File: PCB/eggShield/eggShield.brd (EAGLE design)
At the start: 68.6 x 53.3 mm, 19 parts

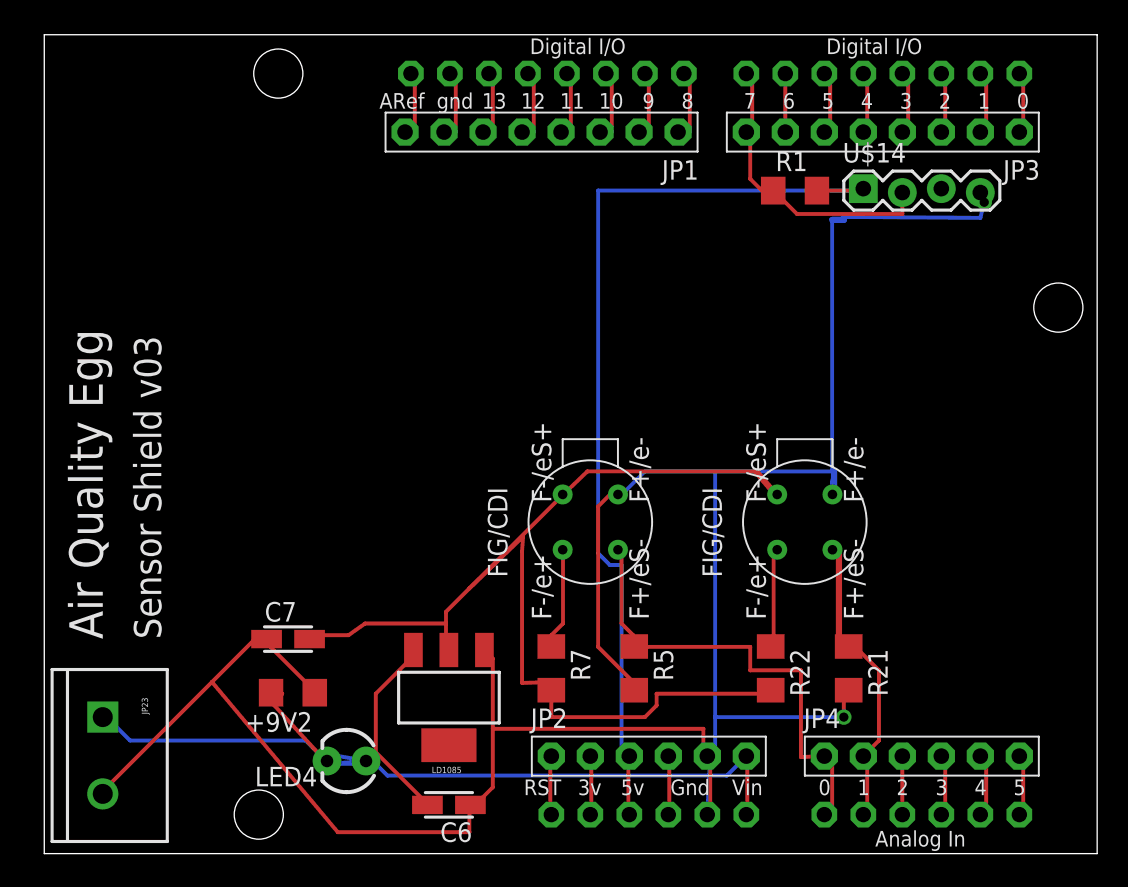
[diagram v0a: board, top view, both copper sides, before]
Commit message: updates to the layout and schematics, bringing in elements of the CMOS breakout module
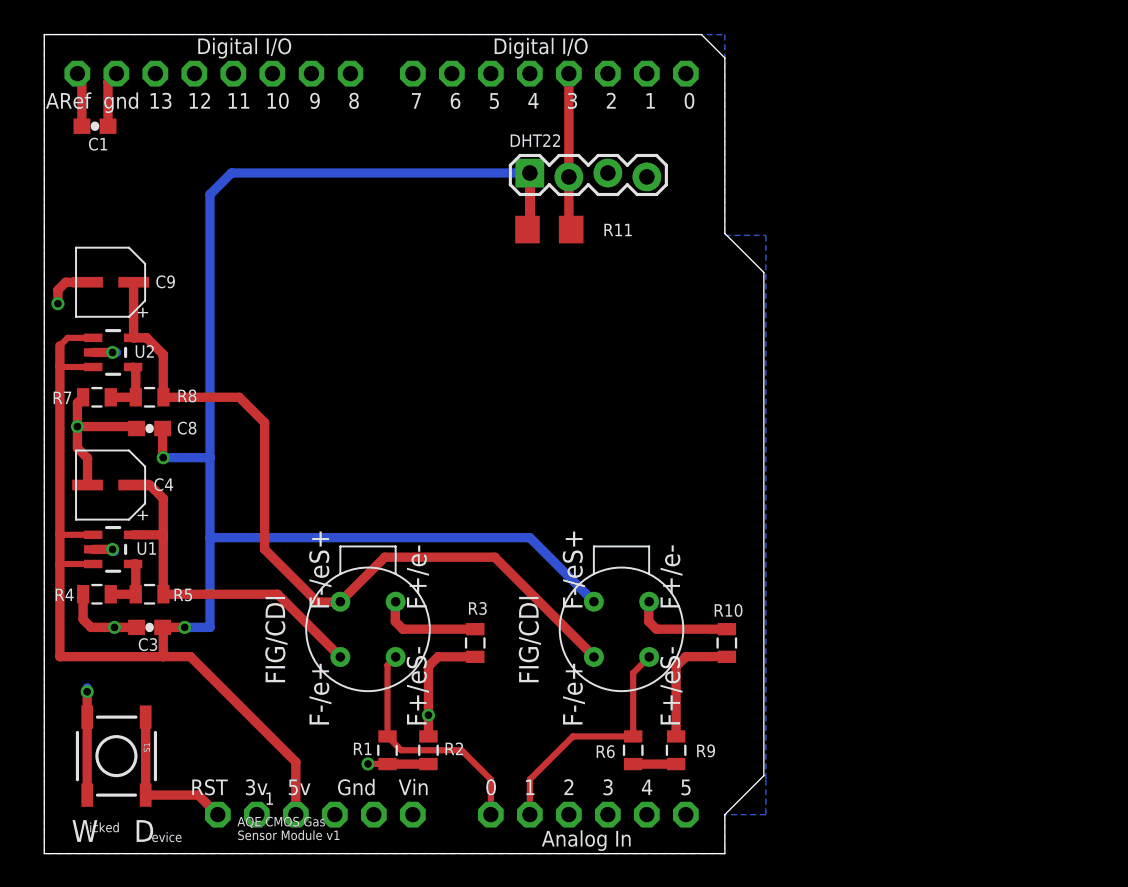
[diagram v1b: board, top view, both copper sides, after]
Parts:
- removed +9V2: 900 ohm, rcl:R1206
- removed C6, C7: 10uF, resistor:CT3216
- removed JP1, JP3: (no value), adafruit:1X08-BIG
- removed JP2, JP4: (no value), adafruit:1X06-BIG
- removed JP23: Screw Terminal, SparkFun:SCREWTERMINAL-5MM-2
- removed LD1085: V_REG_317SMD, SparkFun:SOT223
- removed LED4: (no value), SparkFun:LED3MM
- removed NO2: E2V NO2, ricardo:SR-4
- removed R21: 220k, rcl:R1206
- removed R22: 82 ohm, rcl:R1206
- removed U$13: E2V, ricardo:SR-4
- removed U$14: RHT03, ricardo:1X04_LOCK
- added C1, C3, C8: 0.1uF, SparkFun:0603-CAP
- added C4, C9: 10uF, wicked-device:TYPE-B_ALUMINUM_CAN
- added DHT22: RHT03, ricardo:1X04_LOCK
- added R10, R2, R3, R6, R9: (no value), SparkFun:0805
- added R11: 10k, rcl:R1206
- added R4: 150Ohm, SparkFun:0805
- added R8: 330Ohm, SparkFun:0805
- added S1: (no value), SparkFun:TACTILE_SWITCH_SMD
- added U$4: E2V, ricardo:SR-4
- added U$7: ARDUINO-NOHOLE, adafruit:ARDUINO-NOHOLE
- added U1, U2: V_REG_LDOSMD, SparkFun:SOT23-5
- R1: value 10k -> (none); device rcl:R1206 -> SparkFun:0805
- R5: value 220k -> 330Ohm; device rcl:R1206 -> SparkFun:0805
- R7: value 34 ohm -> 150Ohm; device rcl:R1206 -> SparkFun:0805
- U$2: value ARDUINO-NODIM -> E2V; device adafruit:ARDUINO-NODIM -> ricardo:SR-4
- moved R1 45.1 mm to (22.4, 6.73), turned to 90 degrees
- moved U$2 40.3 mm to (37.6, 14.6), turned to 90 degrees
- moved R7 34.5 mm to (3.43, 29.7), turned to 0 degrees
- moved R5 31.9 mm to (6.86, 16.9), turned to 0 degrees
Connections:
- removed net +5V: JP2.3, R1.2, U$14.VDD, U$2.5V
- removed net +9V: C6.+, JP2.6, JP23.1, LD1085.3, LED4.A, U$2.VIN
- removed net 1.8: +9V2.1, C6.-, C7.-, JP2.5, JP23.2, LD1085.1, NO2.FIGV+/E2V-, R21.2, R5.2, U$13.FIGV+/E2V-, U$14.GND, U$2.GND1
- removed net A3: JP3.8, R1.1, U$14.DATA, U$2.D7
- removed net N$10: JP4.4, U$2.A3
- removed net N$11: JP4.5, U$2.A4
- removed net N$12: JP4.6, U$2.A5
- removed net N$13: JP3.1, U$2.D0
- removed net N$14: JP3.2, U$2.D1
- removed net N$15: JP3.3, U$2.D2
- removed net N$16: JP3.4, U$2.D3
- removed net N$17: JP3.5, U$2.D4
- removed net N$18: JP3.6, U$2.D5
- removed net N$22: JP1.1, U$2.D8
- removed net N$23: JP1.2, U$2.D9
- removed net N$24: +9V2.2, LED4.K
- removed net N$25: JP1.3, U$2.D10
- removed net N$26: JP1.4, U$2.D11
- removed net N$27: JP1.5, U$2.D12
- removed net N$28: JP1.6, U$2.D13
- removed net N$29: JP1.7, U$2.GND
- removed net N$30: JP1.8, U$2.AREF
- removed net N$38: R22.1, U$13.FIGSIG/E2VH+
- removed net N$43: NO2.FIGSIG/E2VH+, R7.1
- removed net N$47: JP4.2, R21.1, U$13.FIGV+/E2VSIG, U$2.A1
- removed net N$5: JP3.7, U$2.D6
- removed net N$50: JP4.1, NO2.FIGV+/E2VSIG, R5.1, U$2.A0
- removed net N$55: JP4.3, U$2.A2
- removed net V+: C7.+, LD1085.2, NO2.FIGG/E2VS+, R22.2, R7.2, U$13.FIGG/E2VS+
- new net /CO_R1_SEL: R6.1, R9.2
- new net /CO_R2_SEL: R10.2, R9.1
- new net /NO2_R1_SEL: R1.1, R2.2
- new net /NO2_R2_SEL: R2.1, R3.2
- new net /RESET: S1.1, S1.2, U$7.RESET
- new net 1.7V: C4.P$1, R5.2, U$4.FIGSIG/E2VH+, U1.5
- new net 2.5V: C9.P$1, R8.2, U$2.FIGSIG/E2VH+, U$4.FIGG/E2VS+, U2.5
- new net 3V: U$7.3V
- new net CO_SENSE: R6.2, U$2.FIGV+/E2VSIG, U$7.A1
- new net D3: DHT22.DATA, R11.1, U$7.D3
- new net GND: C1.1, C3.1, C4.P$2, C8.1, C9.P$2, DHT22.GND, R10.1, R3.1, R4.1, R7.1, S1.3, S1.4, U$2.FIGV+/E2V-, U$4.FIGV+/E2V-, U$7.GND, U$7.GND1, U$7.GND2, U1.2, U2.2
- new net NO2_SENSE: R1.2, U$4.FIGV+/E2VSIG, U$7.A0
- new net SCL: U$7.A5
- new net SDA: U$7.A4
- new net VCC: C3.2, C8.2, DHT22.VDD, R11.2, U$2.FIGG/E2VS+, U$7.5V, U1.1, U1.3, U2.1, U2.3
- new net VIN: U$7.VIN
- net N$1: now also R4.2, R5.1, U1.4; no longer JP2.1, U$2.RESET
- net N$2: now also R7.2, R8.1, U2.4; no longer JP2.2, U$2.3V
- net N$4: now also C1.2, U$7.AREF; no longer JP2.4, U$2.GND2
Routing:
- net 1.8: track 169.6 -> 0.00 mm, vias 2 -> 0
- net VCC: track 0.00 -> 144.7 mm, vias 0 -> 2
- net V+: track 74.5 -> 0.00 mm
- net +9V: track 65.8 -> 0.00 mm
- net +5V: track 62.4 -> 0.00 mm
- net 2.5V: track 0.00 -> 51.2 mm
- net GND: track 0.00 -> 46.0 mm, vias 0 -> 6
- net N$50: track 30.6 -> 0.00 mm
- net 1.7V: track 0.00 -> 23.7 mm
- net N$47: track 20.3 -> 0.00 mm
- net A3: track 19.6 -> 0.00 mm
- net CO_SENSE: track 0.00 -> 15.8 mm
- net NO2_SENSE: track 0.00 -> 15.6 mm
- net /RESET: track 0.00 -> 10.3 mm
- net D3: track 0.00 -> 10.2 mm
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- added copper zone on layer 16, net GND
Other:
- board size 68.6 x 53.3 mm -> 46.9 x 53.3 mm
- board text added: "1"
- board text added: "AQE CMOS Gas"
- board text added: "C4"
- board text added: "C9"
- board text added: "D"
- board text added: "Sensor Module v1"
- board text added: "W"
- board text added: "evice"
- board text added: "icked"
- board text removed: "Air Quality Egg"
- board text removed: "Sensor Shield v03"

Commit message: added 2:1 I2C Multiplexer
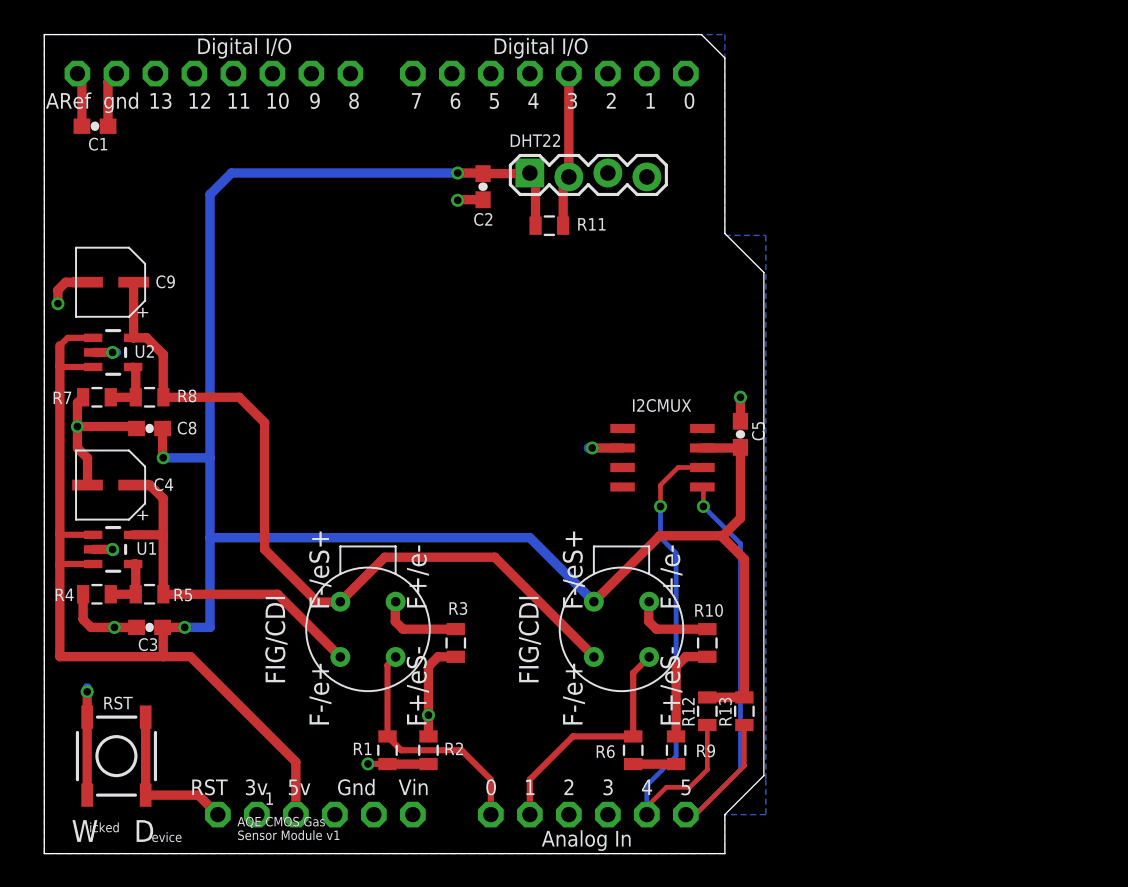
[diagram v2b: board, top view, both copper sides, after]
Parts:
- added C2, C5: 0.1uF, SparkFun:0603-CAP
- added I2CMUX: PCA9540BD, wicked-device:SO8
- added R12, R13: 4.7kOhm, SparkFun:0805
- R11: value 10k -> 10kOhm; device rcl:R1206 -> SparkFun:0805
- moved R10 1.27 mm to (43.2, 13.7)
- moved R3 1.27 mm to (26.8, 13.7)
- moved R11 0.25 mm to (32.9, 40.9), turned to 0 degrees
- renumbered S1 to RST
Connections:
- net D3: now also R11.2; no longer R11.1
- net GND: now also C2.1, C5.1, I2CMUX.6
- net SCL: now also I2CMUX.1, R13.1
- net SDA: now also I2CMUX.2, R12.1
- net VCC: now also C2.2, C5.2, I2CMUX.3, R11.1, R12.2, R13.2; no longer R11.2
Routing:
- net SDA: track 0.00 -> 34.2 mm, vias 0 -> 1
- net SCL: track 0.00 -> 32.0 mm, vias 0 -> 1
- net VCC: track 144.7 -> 175.6 mm, vias 2 -> 3
- net GND: track 46.0 -> 49.2 mm, vias 6 -> 9
- net /CO_R2_SEL: track 8.13 -> 6.86 mm
- net /NO2_R2_SEL: track 7.87 -> 6.60 mm

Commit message: rearranged some layout and routing to improve power filtering
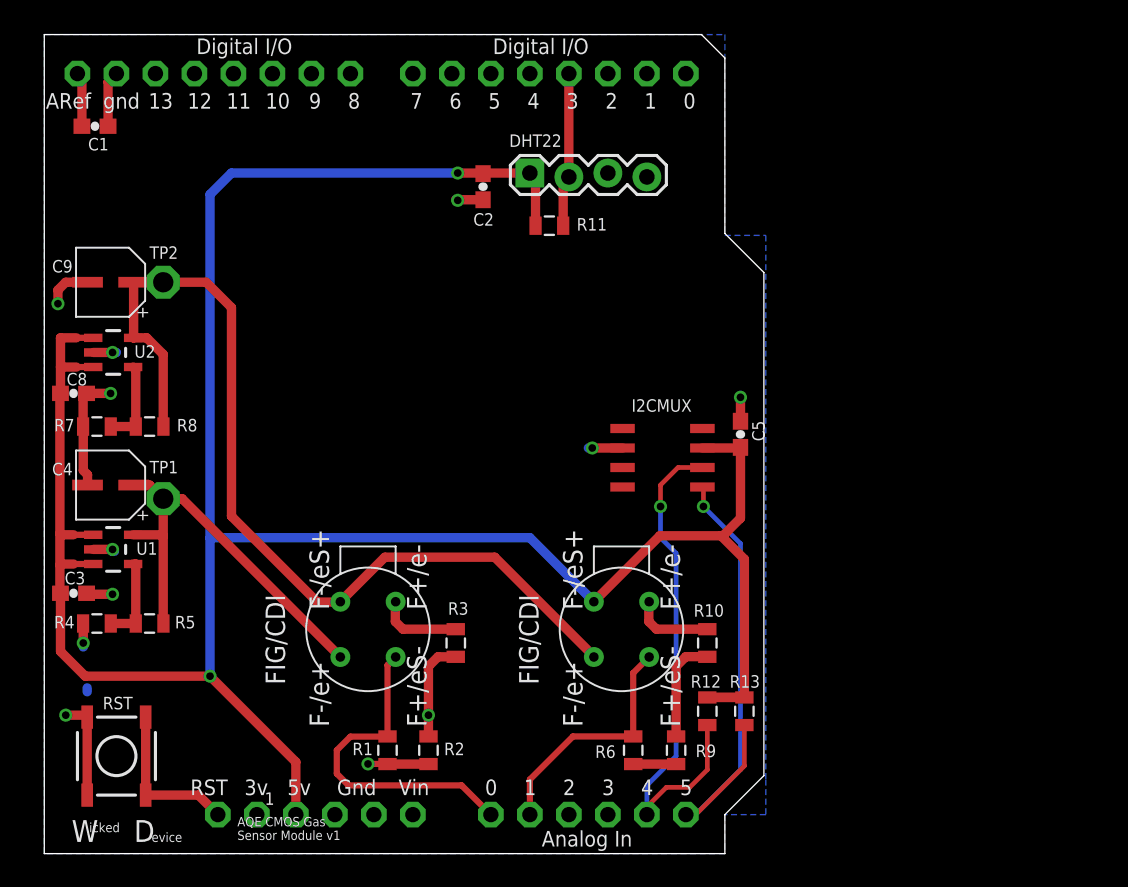
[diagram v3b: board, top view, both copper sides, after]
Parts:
- added TP1, TP2: TPPAD1-13, testpad:P1-13
- R12, R13: value 4.7kOhm -> 1.8kOhm
- moved C8 5.46 mm to (1.91, 30.0), turned to 180 degrees
- moved C3 5.43 mm to (1.91, 17.0), turned to 180 degrees
- moved R7 1.91 mm to (3.43, 27.8)
- moved R8 1.91 mm to (6.86, 27.8)
- moved R4 1.90 mm to (3.43, 15.0)
- moved R5 1.90 mm to (6.86, 15.0)
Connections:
- net 1.7V: now also TP1.TP
- net 2.5V: now also TP2.TP
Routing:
- net 2.5V: track 51.2 -> 61.3 mm
- net VCC: track 175.6 -> 168.9 mm, vias 3 -> 2
- net NO2_SENSE: track 15.6 -> 21.7 mm
- net GND: track 49.2 -> 44.6 mm, vias 9 -> 10
- net 1.7V: track 23.7 -> 28.2 mm
- net N$2: track 3.67 -> 5.58 mm
- net N$1: track 3.82 -> 5.73 mm

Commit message: some minor changes to component placement, routing, and silk screen
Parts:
- moved TP1 1.02 mm to (8.76, 23.1)
- moved TP2 1.02 mm to (8.76, 37.2)
- moved C2 0.64 mm to (29.2, 43.4)
- moved DHT22 0.64 mm to (32.3, 44.2)
- moved R2 0.64 mm to (25.7, 6.73)
- moved C4 0.64 mm to (4.95, 24.0)
- moved C9 0.64 mm to (4.95, 37.2)
- moved R5 0.64 mm to (7.49, 15.0)
- moved R8 0.64 mm to (7.49, 27.8)
- moved R4 0.64 mm to (4.06, 15.0)
- moved R7 0.64 mm to (4.06, 27.8)
- moved C3 0.64 mm to (2.54, 17.0)
- moved C8 0.64 mm to (2.54, 30.0)
- moved C1 0.63 mm to (3.94, 47.4)
- moved RST 0.63 mm to (5.33, 6.35)
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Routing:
- net SDA: track 34.2 -> 34.8 mm
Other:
- board size 46.9 x 53.3 mm -> 47.5 x 53.3 mm
- board text added: "1.7V"
- board text added: "2.5V"
- board text added: "Air Quality Egg"
- board text added: "Sensor Interface Shield v1"
- board text removed: "AQE CMOS Gas"
- board text removed: "Sensor Module v1"

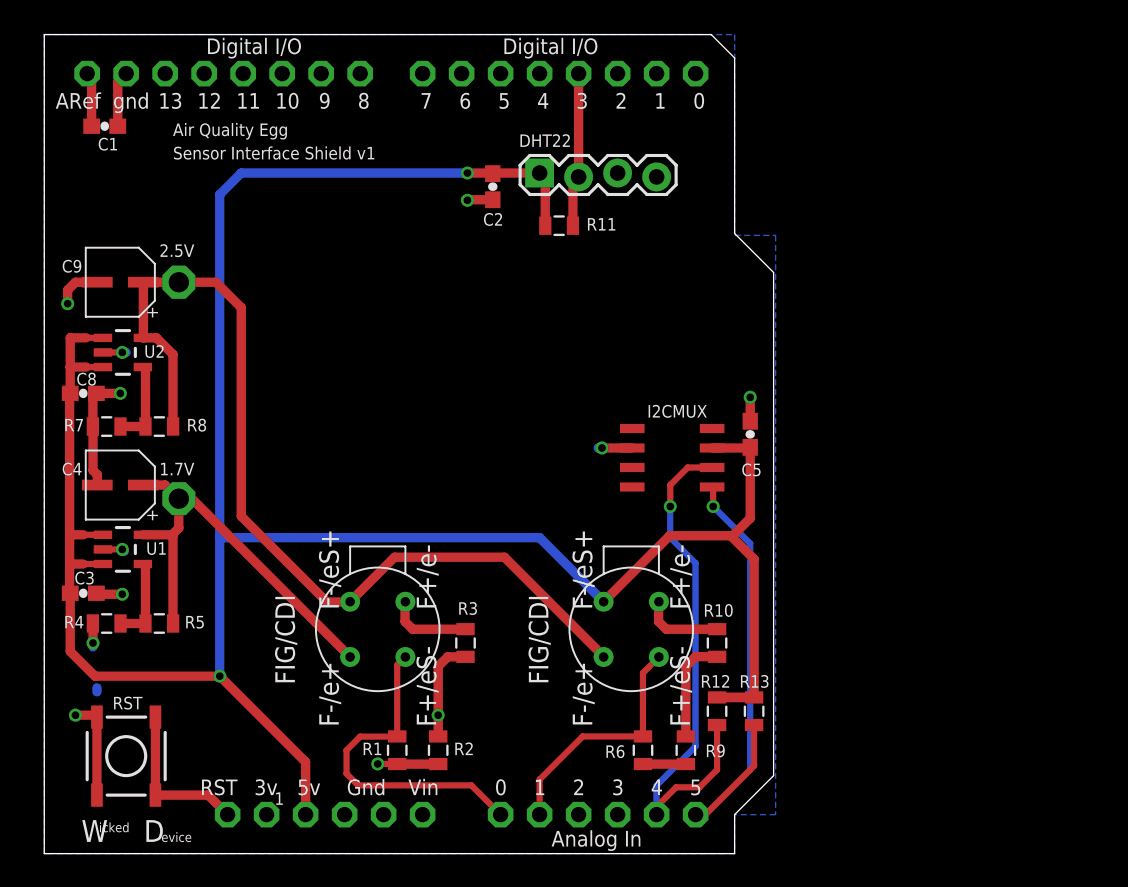
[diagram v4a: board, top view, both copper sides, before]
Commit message: added 4-pin connectors, needs to be checked against cabling; also noticed the range selection resistor taps need to be routed to arduino pins as well
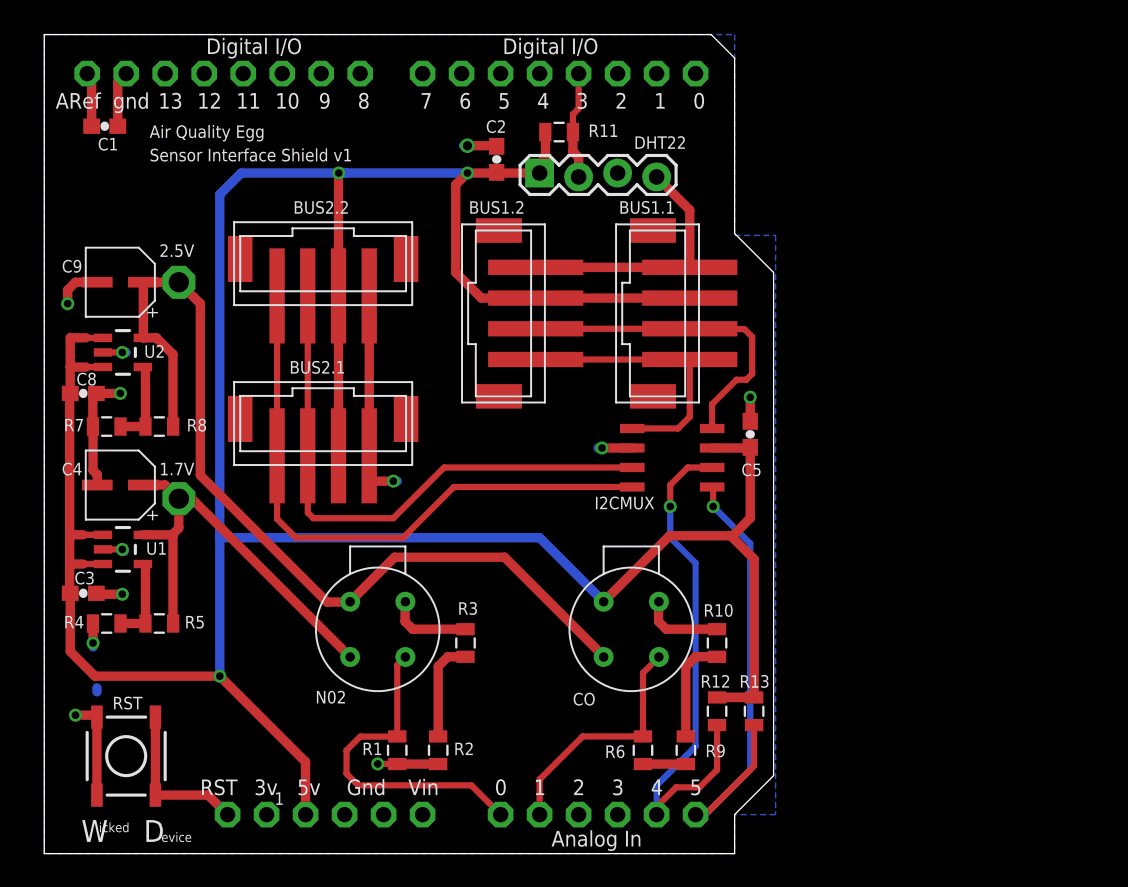
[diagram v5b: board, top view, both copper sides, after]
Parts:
- added BUS1.1, BUS1.2, BUS2.1, BUS2.2: 4-PIN-SMT, wicked-device:1775470-4
- moved R11 6.10 mm to (33.5, 47.0)
- moved C2 1.80 mm to (29.5, 45.2), turned to 270 degrees
- renumbered U$2 to CO, U$4 to N02
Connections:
- new net SCL0: BUS1.1.1, BUS1.2.1, I2CMUX.5
- new net SCL1: BUS2.1.1, BUS2.2.1, I2CMUX.8
- new net SDA0: BUS1.1.2, BUS1.2.2, I2CMUX.4
- new net SDA1: BUS2.1.2, BUS2.2.2, I2CMUX.7
- net GND: now also BUS1.1.4, BUS1.2.4, BUS2.1.4, BUS2.2.4
- net VCC: now also BUS1.1.3, BUS1.2.3, BUS2.1.3, BUS2.2.3
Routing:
- net VCC: track 168.9 -> 209.2 mm, vias 2 -> 3
- net SCL1: track 0.00 -> 39.5 mm
- net SDA1: track 0.00 -> 36.8 mm
- net GND: track 44.6 -> 75.6 mm, vias 10 -> 11
- net SDA0: track 0.00 -> 21.7 mm
- net SCL0: track 0.00 -> 17.8 mm
- net D3: track 10.1 -> 7.04 mm
- net 2.5V: track 61.3 -> 59.8 mm
- net /NO2_R2_SEL: vias 1 -> 0
